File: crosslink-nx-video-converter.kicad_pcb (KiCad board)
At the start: 2 copper layers, 114 parts, among them J1 WE_68715014522, J2 WE_68715014522, U1 AP7330-W5-7, U2 AP7330-W5-7, U3 AP7330-W5-7, U4 AP62301WU-7, U5 AP62301WU-7, U6 AP62301WU-7, U7 MT41K128M16JT-125_K, U8 NCV51200MNTXG, U9 LIFCL-40-9BG256C

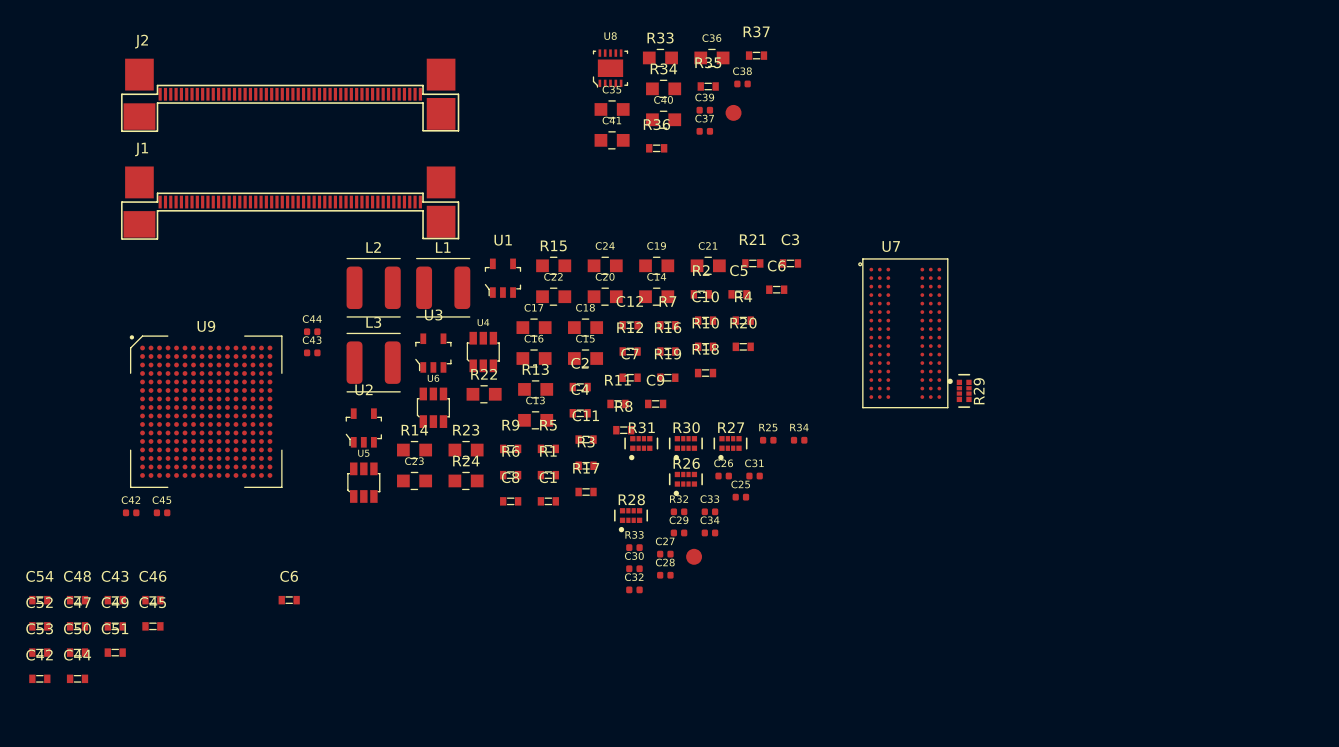
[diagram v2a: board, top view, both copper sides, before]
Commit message: Connected EN pins on PSU schematic
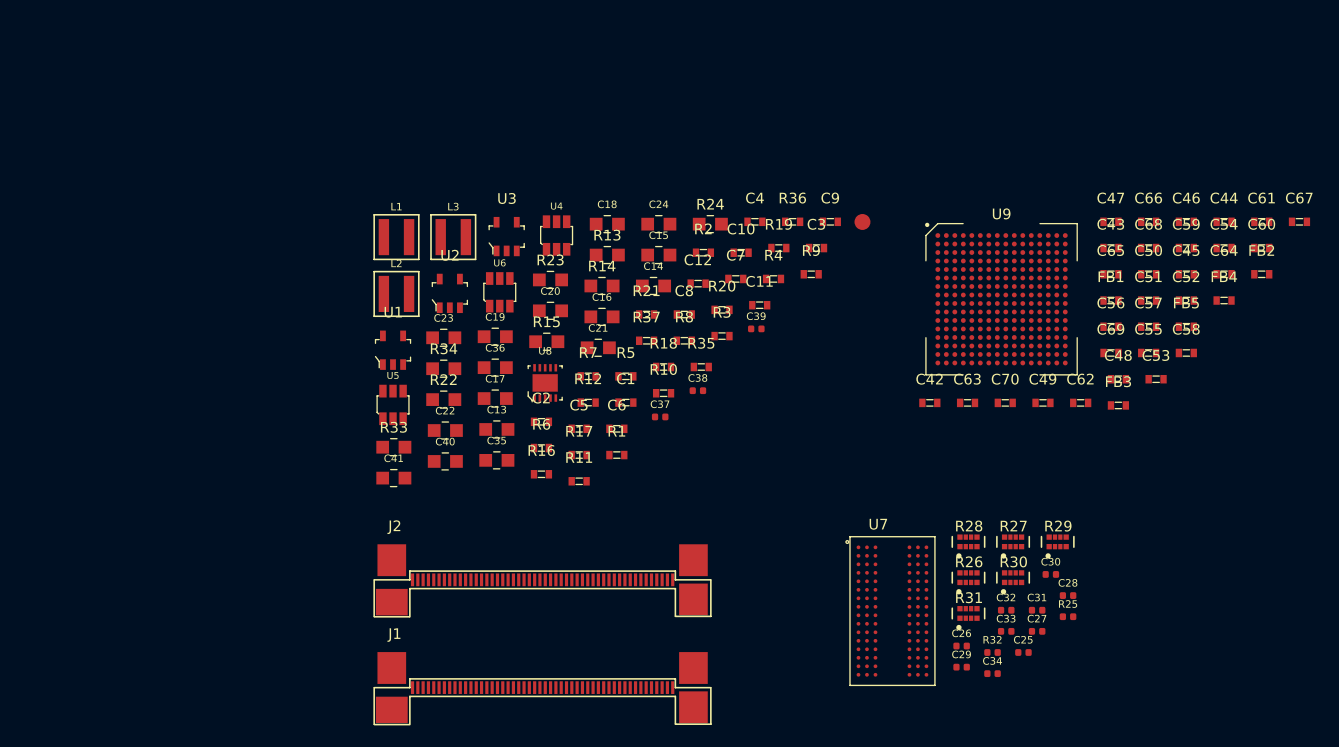
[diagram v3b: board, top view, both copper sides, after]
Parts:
- removed the C42 at (88.7, 97.1)
- removed the C42 at (80.1, 112.7)
- removed the C43 at (87.2, 105.3)
- removed the C43 at (105.8, 82.0)
- removed the C44 at (83.7, 112.7)
- removed the C44 at (105.8, 80.0)
- removed the C45 at (90.8, 107.8)
- removed the C45 at (91.6, 97.1)
- removed the C6 at (103.6, 105.3)
- removed the C6 at (149.5, 76.1)
- removed the R33 at (136.1, 100.4)
- removed the R33 at (138.6, 54.2)
- removed the R34 at (151.6, 90.2)
- removed the R34 at (138.8, 57.2)
- removed TP1: TP, antmicro-footprints:TP-R-1.5
- added C42: C_100n_0603, antmicro-footprints:0603-cap, F.Cu at (163.9, 86.7)
- added C43: C_100n_0603, antmicro-footprints:0603-cap, F.Cu at (181.0, 72.2)
- added C44: C_100n_0603, antmicro-footprints:0603-cap, F.Cu at (191.6, 69.7)
- added C45: C_100n_0603, antmicro-footprints:0603-cap, F.Cu at (188.1, 74.6)
- added C55: C_100n_0603, antmicro-footprints:0603-cap, F.Cu at (184.5, 82.0)
- added C56: C_10u_0603, antmicro-footprints:0603-cap, F.Cu at (181.0, 79.6)
- added C57: C_10u_0603, antmicro-footprints:0603-cap, F.Cu at (184.5, 79.6)
- added C58: C_10u_0603, antmicro-footprints:0603-cap, F.Cu at (188.1, 82.0)
- added C59: C_10u_0603, antmicro-footprints:0603-cap, F.Cu at (188.1, 72.2)
- added C6: C_10u_0603, antmicro-footprints:0603-cap, F.Cu at (134.4, 89.2)
- added C60: C_10u_0603, antmicro-footprints:0603-cap, F.Cu at (195.2, 72.2)
- added C61: C_1u_0603, antmicro-footprints:0603-cap, F.Cu at (195.2, 69.7)
- added C62: C_10u_0603, antmicro-footprints:0603-cap, F.Cu at (178.1, 86.7)
- added C63: C_100n_0603, antmicro-footprints:0603-cap, F.Cu at (167.5, 86.7)
- added C64: C_100n_0603, antmicro-footprints:0603-cap, F.Cu at (191.6, 74.6)
- added C65: C_100n_0603, antmicro-footprints:0603-cap, F.Cu at (181.0, 74.6)
- added C66: C_100n_0603, antmicro-footprints:0603-cap, F.Cu at (184.5, 69.7)
- added C67: C_100n_0603, antmicro-footprints:0603-cap, F.Cu at (198.7, 69.7)
- added C68: C_100n_0603, antmicro-footprints:0603-cap, F.Cu at (184.5, 72.2)
- added C69: C_100n_0603, antmicro-footprints:0603-cap, F.Cu at (181.0, 82.0)
- added C70: C_100n_0603, antmicro-footprints:0603-cap, F.Cu at (171.0, 86.7)
- added FB1: BLM18PG121SN1D, antmicro-footprints:0603-res, F.Cu at (181.0, 77.1)
- added FB2: BLM18PG121SN1D, antmicro-footprints:0603-res, F.Cu at (195.2, 74.6)
- added FB3: BLM18PG121SN1D, antmicro-footprints:0603-res, F.Cu at (181.7, 87.0)
- added FB4: BLM18PG121SN1D, antmicro-footprints:0603-res, F.Cu at (191.6, 77.1)
- added FB5: BLM18PG121SN1D, antmicro-footprints:0603-res, F.Cu at (188.1, 79.6)
- added R33: R_0R_0805, antmicro-footprints:0805-res, F.Cu at (113.5, 90.9)
- added R34: R_0R_0805, antmicro-footprints:0805-res, F.Cu at (118.2, 83.5)
- L1, L2, L3: value DJNR5020-3R3-S -> XEL4030-332MEC; footprint crosslink-nx-video-converter:L_4.9x4.9mm -> antmicro-footprints:Coilcraft-XEL4030
- moved C54 116.3 mm to (191.6, 72.2)
- moved C52 112.2 mm to (188.1, 77.1)
- moved C53 108.2 mm to (185.2, 84.5)
- moved C50 107.0 mm to (184.5, 74.6)
- moved C47 104.5 mm to (181.0, 69.7)
- moved C46 103.6 mm to (188.1, 69.7)
- moved C51 102.8 mm to (184.5, 77.1)
- moved C48 100.2 mm to (181.7, 84.5)
- moved C49 89.8 mm to (174.6, 86.7)
- moved U9 75.6 mm to (170.7, 77.0)
- moved J2 51.5 mm to (127.5, 102.8)
- moved J1 51.5 mm to (127.5, 112.9)
- moved C30 39.2 mm to (175.3, 102.9)
- moved C40 38.2 mm to (118.3, 92.2)
- moved C28 38.0 mm to (176.9, 104.9)
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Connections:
- C46 pad 1: +1V8 -> +1V35
- C47 pad 1: +1V8 -> /FPGA/VCC_AUX
- C48 pad 1: +1V8 -> /FPGA/VCC_AUX
- C50 pad 1: +1V8 -> /FPGA/VCC_AUX
- C52 pad 1: +1V8 -> /FPGA/VCC_AUX
- C54 pad 1: +1V8 -> /FPGA/VCC_AUX
- U9 pad A1: Net-(U9-PadA1) -> GND
- U9 pad A10: Net-(U9-PadA10) -> GND
- U9 pad A13: Net-(U9-PadA10) -> GND
- U9 pad A16: Net-(U9-PadA10) -> GND
- U9 pad A2: unconnected-(U9-PadA2) -> /FPGA/VCC_PLLDPHY
- U9 pad A8: Net-(U9-PadA1) -> GND
- U9 pad B10: Net-(U9-PadA10) -> GND
- U9 pad B14: Net-(U9-PadA10) -> GND
- U9 pad B8: Net-(U9-PadA1) -> GND
- U9 pad C10: Net-(U9-PadC10) -> GND
- U9 pad C3: Net-(U9-PadA1) -> GND
- U9 pad C4: unconnected-(U9-PadC4) -> /FPGA/VCC_DPHY
- U9 pad C5: unconnected-(U9-PadC5) -> /FPGA/VCC_PLLDPHY
- U9 pad C6: Net-(U9-PadA1) -> GND
- U9 pad C7: unconnected-(U9-PadC7) -> /FPGA/VCC_DPHY
- U9 pad C8: unconnected-(U9-PadC8) -> /FPGA/VCC_ADPHY
- U9 pad C9: Net-(U9-PadC10) -> GND
- U9 pad D14: Net-(U9-PadC10) -> GND
- U9 pad D3: Net-(U9-PadA1) -> GND
- U9 pad D8: Net-(U9-PadC10) -> GND
- U9 pad E3: unconnected-(U9-PadE3) -> /FPGA/VCC_ADPHY
- U9 pad E7: Net-(U9-PadC10) -> GND
- U9 pad E8: Net-(U9-PadC10) -> GND
- U9 pad F12: Net-(U9-PadC10) -> GND
- U9 pad F3: Net-(U9-PadA1) -> GND
- U9 pad F7: +1V8 -> /FPGA/VCC_AUXA
- U9 pad F8: +1V8 -> /FPGA/VCC_AUX
- U9 pad G1: Net-(U9-PadA1) -> GND
- U9 pad G2: Net-(U9-PadC10) -> GND
- U9 pad G5: Net-(U9-PadC10) -> GND
- U9 pad G7: +1V8 -> /FPGA/VCC_AUX
- U9 pad G8: Net-(U9-PadC10) -> GND
- U9 pad H8: Net-(U9-PadC10) -> GND
- U9 pad H9: Net-(U9-PadC10) -> GND
- U9 pad J14: Net-(U9-PadC10) -> GND
- U9 pad J3: Net-(U9-PadC10) -> GND
- U9 pad J7: Net-(U9-PadC10) -> GND
- U9 pad J8: Net-(U9-PadC10) -> GND
- U9 pad J9: Net-(U9-PadC10) -> GND
- U9 pad K10: +1V8 -> /FPGA/VCC_AUX
- U9 pad K8: +1V8 -> /FPGA/VCC_AUX
- U9 pad K9: unconnected-(U9-PadK9) -> 1V0_Power
- U9 pad M5: Net-(U9-PadC10) -> GND
- U9 pad M6: +1V8 -> /FPGA/VCC_AUX
- U9 pad N7: Net-(U9-PadC10) -> GND
- U9 pad P13: Net-(U9-PadC10) -> GND
- U9 pad T1: Net-(U9-PadC10) -> GND
- U9 pad T16: Net-(U9-PadC10) -> GND

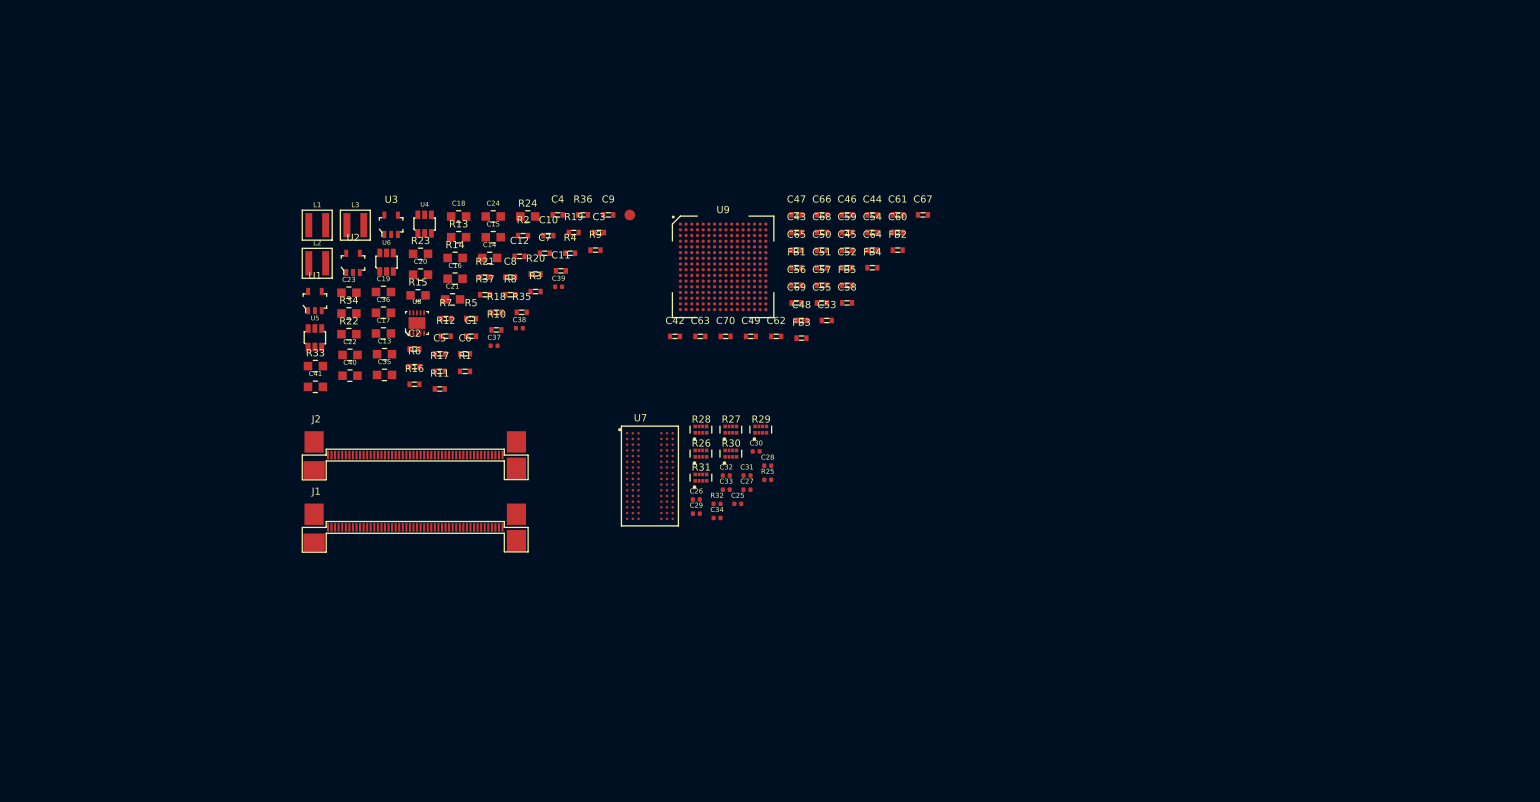
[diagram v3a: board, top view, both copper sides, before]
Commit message: Connected Semtech to the power supply, cable driver and the FPGA
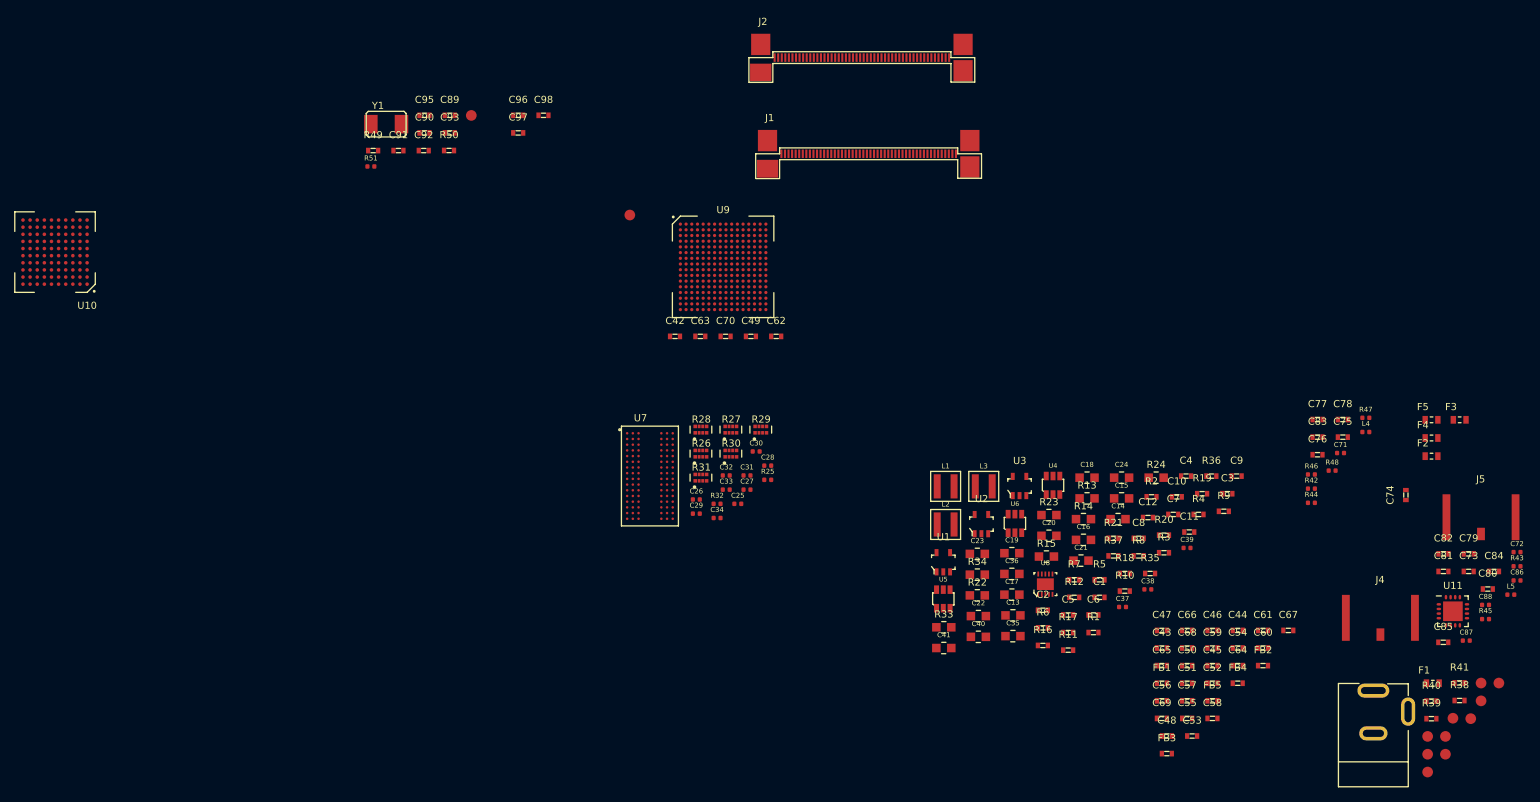
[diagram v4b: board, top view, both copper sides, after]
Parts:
- added C71: C_1u_0402, antmicro-footprints:0402-cap, F.Cu at (257.3, 103.1)
- added C72: C_1u_0402, antmicro-footprints:0402-cap, F.Cu at (282.1, 117.0)
- added C73: C_100n_0603, antmicro-footprints:0603-cap, F.Cu at (275.3, 119.7)
- added C74: C_100n_0603, antmicro-footprints:0603-cap, F.Cu at (266.5, 109.0)
- added C75: C_100n_0603, antmicro-footprints:0603-cap, F.Cu at (257.6, 100.9)
- added C76: C_100n_0603, antmicro-footprints:0603-cap, F.Cu at (254.1, 103.3)
- added C77: C_100n_0603, antmicro-footprints:0603-cap, F.Cu at (254.1, 98.4)
- added C78: C_100n_0603, antmicro-footprints:0603-cap, F.Cu at (257.6, 98.4)
- added C79: C_100n_0603, antmicro-footprints:0603-cap, F.Cu at (275.3, 117.2)
- added C80: C_100n_0603, antmicro-footprints:0603-cap, F.Cu at (278.0, 122.2)
- added C81: C_100n_0603, antmicro-footprints:0603-cap, F.Cu at (271.8, 119.7)
- added C82: C_100n_0603, antmicro-footprints:0603-cap, F.Cu at (271.8, 117.2)
- added C83: C_100n_0603, antmicro-footprints:0603-cap, F.Cu at (254.1, 100.9)
- added C84: C_100n_0603, antmicro-footprints:0603-cap, F.Cu at (278.9, 119.7)
- added C85: C_100n_0603, antmicro-footprints:0603-cap, F.Cu at (271.8, 129.7)
- added C86: C_10n_0402, antmicro-footprints:0402-cap, F.Cu at (282.1, 121.0)
- added C87: C_4u7_0402, antmicro-footprints:0402-cap, F.Cu at (275.0, 129.4)
- added C88: C_4u7_0402, antmicro-footprints:0402-cap, F.Cu at (277.7, 124.4)
- added C89: C_33p_0603, antmicro-footprints:0603-cap, F.Cu at (132.3, 55.7)
- added C90: C_33p_0603, antmicro-footprints:0603-cap, F.Cu at (128.8, 58.2)
- added C91: C_470n_0603, antmicro-footprints:0603-cap, F.Cu at (125.1, 60.6)
- added C92: C_47n_0603, antmicro-footprints:0603-cap, F.Cu at (128.7, 60.6)
- added C93: C_470n_0603, antmicro-footprints:0603-cap, F.Cu at (132.3, 58.2)
- added C95: C_33u_0603, antmicro-footprints:0603-cap, F.Cu at (128.8, 55.7)
- added C96: C_100n_0603, antmicro-footprints:0603-cap, F.Cu at (141.9, 55.7)
- added C97: C_100n_0603, antmicro-footprints:0603-cap, F.Cu at (141.9, 58.2)
- added C98: C_100n_0603, antmicro-footprints:0603-cap, F.Cu at (145.5, 55.7)
- added F1: 04671.25NR, antmicro-footprints:0603-Fuse-Littelfuse-0467, F.Cu at (270.3, 135.4)
- added F2: 04671.25NR, antmicro-footprints:0603-Fuse-Littelfuse-0467, F.Cu at (270.1, 103.5)
- added F3: 04671.25NR, antmicro-footprints:0603-Fuse-Littelfuse-0467, F.Cu at (274.1, 98.4)
- added F4: 04671.25NR, antmicro-footprints:0603-Fuse-Littelfuse-0467, F.Cu at (270.1, 101.0)
- added F5: 04671.25NR, antmicro-footprints:0603-Fuse-Littelfuse-0467, F.Cu at (270.1, 98.4)
- added J3: DC_SOCKET, antmicro-footprints:DC_SOCKET, F.Cu at (261.9, 150.1)
- added J4: 031-70526-21, antmicro-footprints:BNC_Edge_Conn, F.Cu at (262.9, 128.6)
- added J5: 031-70526-21, antmicro-footprints:BNC_Edge_Conn, F.Cu at (277.0, 114.5)
- added L4: L_0402_6n2, antmicro-footprints:0402-cap, F.Cu at (260.9, 100.2)
- added L5: L_0402_6n2, antmicro-footprints:0402-cap, F.Cu at (281.2, 123.0)
- added R38: R_0R_0603, antmicro-footprints:0603-res, F.Cu at (274.0, 137.8)
- added R39: R_0R_0603, antmicro-footprints:0603-res, F.Cu at (270.1, 140.4)
- added R40: R_0R_0603, antmicro-footprints:0603-res, F.Cu at (270.1, 137.9)
- added R41: R_0R_0603, antmicro-footprints:0603-res, F.Cu at (274.0, 135.4)
- added R42: R_75R_0402, antmicro-footprints:0402-res, F.Cu at (253.2, 108.1)
- added R43: R_75R_0402, antmicro-footprints:0402-res, F.Cu at (282.1, 119.0)
- added R44: R_37R4_0402, antmicro-footprints:0402-res, F.Cu at (253.2, 110.1)
- added R45: R_75R_0402, antmicro-footprints:0402-res, F.Cu at (277.7, 126.4)
- added R46: R_75R_0402, antmicro-footprints:0402-res, F.Cu at (253.2, 106.1)
- added R47: R_75R_0402, antmicro-footprints:0402-res, F.Cu at (260.9, 98.2)
- added R48: R_75R_0402, antmicro-footprints:0402-res, F.Cu at (256.1, 105.6)
- added R49: R_100k_0603, antmicro-footprints:0603-res, F.Cu at (121.5, 60.6)
- added R50: R_100k_0603, antmicro-footprints:0603-res, F.Cu at (132.2, 60.6)
- added R51: R_105R_0402, antmicro-footprints:0402-res, F.Cu at (121.2, 62.9)
- added TP1: TP, antmicro-footprints:TP-R-1.5, F.Cu at (279.6, 135.4)
- added TP10: TP, antmicro-footprints:TP-R-1.5, F.Cu at (272.1, 145.4)
- added TP11: TP, antmicro-footprints:TP-R-1.5, F.Cu at (269.6, 147.9)
- added TP12: TP, antmicro-footprints:TP-R-1.5, F.Cu at (135.3, 55.7)
- added TP3: TP, antmicro-footprints:TP-R-1.5, F.Cu at (269.6, 142.9)
- added TP4: TP, antmicro-footprints:TP-R-1.5, F.Cu at (275.6, 140.4)
- added TP5: TP, antmicro-footprints:TP-R-1.5, F.Cu at (272.1, 142.9)
- added TP6: TP, antmicro-footprints:TP-R-1.5, F.Cu at (273.1, 140.3)
- added TP7: TP, antmicro-footprints:TP-R-1.5, F.Cu at (277.1, 137.9)
- added TP8: TP, antmicro-footprints:TP-R-1.5, F.Cu at (269.6, 145.4)
- added TP9: TP, antmicro-footprints:TP-R-1.5, F.Cu at (277.1, 135.4)
- added U10: GS2971A, antmicro-footprints:BGA100_11x11mm, F.Cu at (76.9, 74.9)
- added U11: GS2988, antmicro-footprints:QFN-16_EP_4x4_Pitch0.65mm, F.Cu at (273.1, 125.3)
- added Y1: ABM7_27.000MH_D2Y_T, antmicro-footprints:ABM7_OSC, F.Cu at (123.4, 56.9)
- moved R1 95.5 mm to (222.7, 128.3)
- moved R10 95.5 mm to (227.1, 122.5)
- moved R16 95.5 mm to (215.6, 130.1)
- moved R18 95.5 mm to (227.1, 120.0)
- moved C12 95.5 mm to (230.3, 112.2)
- moved C2 95.5 mm to (215.6, 125.2)
- moved C20 95.5 mm to (216.4, 114.7)
- moved C21 95.5 mm to (220.9, 118.2)
- moved C4 95.5 mm to (235.7, 106.3)
- moved C40 95.5 mm to (206.5, 128.9)
- moved C6 95.5 mm to (222.7, 125.8)
- moved R15 95.5 mm to (216.1, 117.6)
- moved R19 95.5 mm to (237.9, 108.8)
- moved R2 95.5 mm to (230.8, 109.2)
- moved R20 95.5 mm to (232.6, 114.6)
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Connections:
- net 3V3_FFC1 renamed Net-(J1-Pad47)
- net 3V3_FFC2 renamed Net-(J2-Pad47)
- J1 pad 49: 5V0_FFC1 -> Net-(J1-Pad49)
- J1 pad 50: 5V0_FFC1 -> Net-(J1-Pad49)
- J2 pad 49: 5V0_FFC1 -> Net-(J2-Pad49)
- J2 pad 50: 5V0_FFC1 -> Net-(J2-Pad49)
- U1 pad 3: unconnected-(U1-Pad3) -> Net-(U1-Pad3)
- U2 pad 3: unconnected-(U2-Pad3) -> Net-(U2-Pad3)
- U3 pad 3: unconnected-(U3-Pad3) -> Net-(U3-Pad3)
- U4 pad 5: unconnected-(U4-Pad5) -> Net-(U4-Pad5)
- U5 pad 5: unconnected-(U5-Pad5) -> Net-(U5-Pad5)
- U6 pad 5: unconnected-(U6-Pad5) -> Net-(U6-Pad5)
- U8 pad 7: unconnected-(U8-Pad7) -> Net-(U8-Pad7)
- U9 pad F5: unconnected-(U9-PadF5) -> +3V3
- U9 pad G3: unconnected-(U9-PadG3) -> SDI_STAT5
- U9 pad H1: unconnected-(U9-PadH1) -> SDI_D4
- U9 pad H2: unconnected-(U9-PadH2) -> SDI_D5
- U9 pad H3: unconnected-(U9-PadH3) -> SDI_D3
- U9 pad H4: unconnected-(U9-PadH4) -> SDI_D2
- U9 pad H5: unconnected-(U9-PadH5) -> SDI_D1
- U9 pad H6: unconnected-(U9-PadH6) -> SDI_D0
- U9 pad J1: unconnected-(U9-PadJ1) -> SDI_D7
- U9 pad J2: unconnected-(U9-PadJ2) -> SDI_D8
- U9 pad J4: unconnected-(U9-PadJ4) -> +3V3
- U9 pad J5: unconnected-(U9-PadJ5) -> SDI_D6
- U9 pad J6: unconnected-(U9-PadJ6) -> SDI_PCLK
- U9 pad K1: unconnected-(U9-PadK1) -> SDI_D9
- U9 pad K2: unconnected-(U9-PadK2) -> SDI_D10
- U9 pad K3: unconnected-(U9-PadK3) -> SDI_D12
- U9 pad K4: unconnected-(U9-PadK4) -> SDI_D11
- U9 pad K5: unconnected-(U9-PadK5) -> SDI_D14
- U9 pad K6: unconnected-(U9-PadK6) -> SDI_D13
- U9 pad L1: unconnected-(U9-PadL1) -> SDI_D15
- U9 pad L2: unconnected-(U9-PadL2) -> SDI_D16
- U9 pad L3: unconnected-(U9-PadL3) -> SDI_STAT2
- U9 pad L4: unconnected-(U9-PadL4) -> SDI_D19
- U9 pad L5: unconnected-(U9-PadL5) -> SDI_STAT0
- U9 pad M1: unconnected-(U9-PadM1) -> SDI_D17
- U9 pad M2: unconnected-(U9-PadM2) -> SDI_D18
- U9 pad M3: unconnected-(U9-PadM3) -> SDI_STAT1
- U9 pad N1: unconnected-(U9-PadN1) -> SDI_STAT4
- U9 pad N2: unconnected-(U9-PadN2) -> SDI_STAT3
